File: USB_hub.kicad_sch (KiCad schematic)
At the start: 0 parts

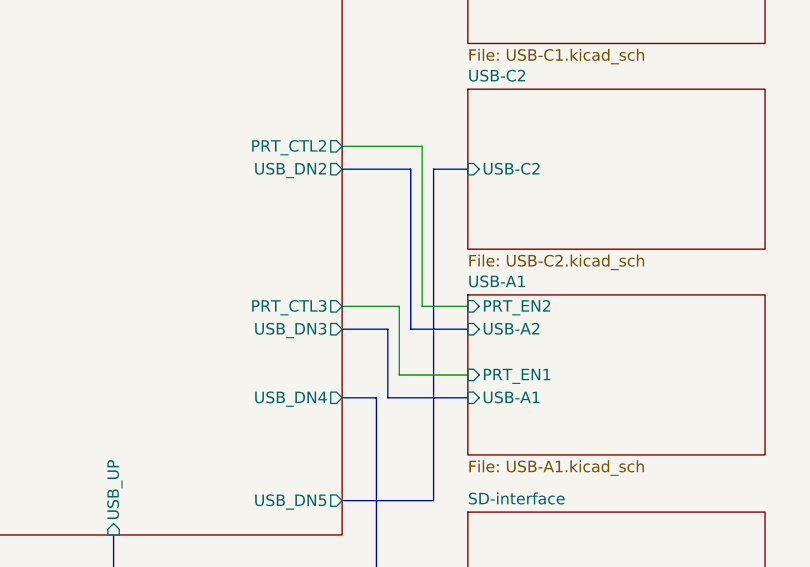
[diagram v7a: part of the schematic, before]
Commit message: Rearrange of the component placement, scheme changes for better routing
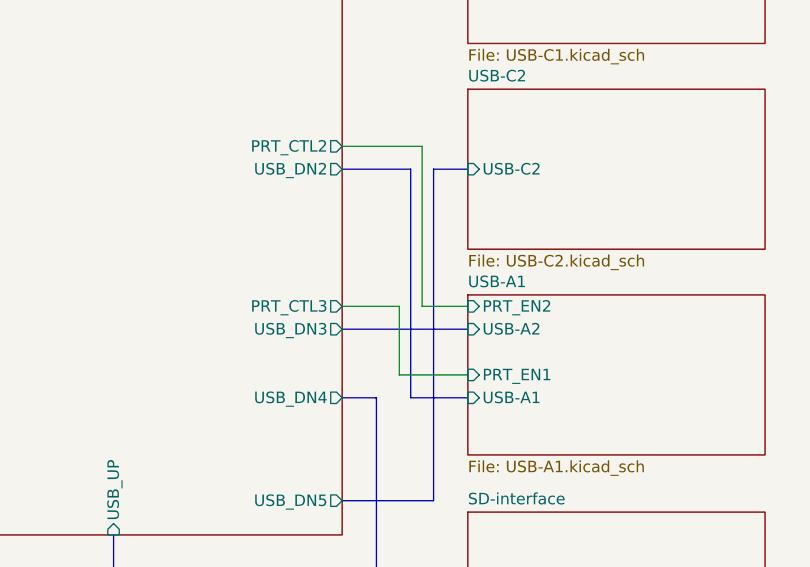
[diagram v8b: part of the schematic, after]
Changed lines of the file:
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@@
-	(bus
-		(pts
-			(xy 278.13 52.07) (xy 278.13 69.85)
-		)
-		(stroke
-			(width 0)
-			(type default)
-		)
-	)
 	(bus
 		(pts
@@
 	(bus
 		(pts
-			(xy 278.13 69.85) (xy 284.48 69.85)
+			(xy 278.13 52.07) (xy 278.13 77.47)
 		)
 		(stroke
@@
 	(bus
 		(pts
-			(xy 275.59 69.85) (xy 275.59 77.47)
-		)
-		(stroke
-			(width 0)
-			(type default)
-		)
-	)
-	(bus
-		(pts
 			(xy 274.32 77.47) (xy 274.32 99.06)
 		)
@@
 	(bus
 		(pts
-			(xy 270.51 69.85) (xy 275.59 69.85)
+			(xy 270.51 69.85) (xy 284.48 69.85)
 		)
 		(stroke
@@
 	(bus
 		(pts
-			(xy 275.59 77.47) (xy 284.48 77.47)
+			(xy 278.13 77.47) (xy 284.48 77.47)
 		)
 		(stroke
